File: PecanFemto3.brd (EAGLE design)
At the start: 28.9 x 17 mm, 43 parts, among them IC1 SPV1040T, IC3 EVA7M, IC4 SI4060/3, IC5 LPC824M201JHI33E, U1 TPS62203DBVT

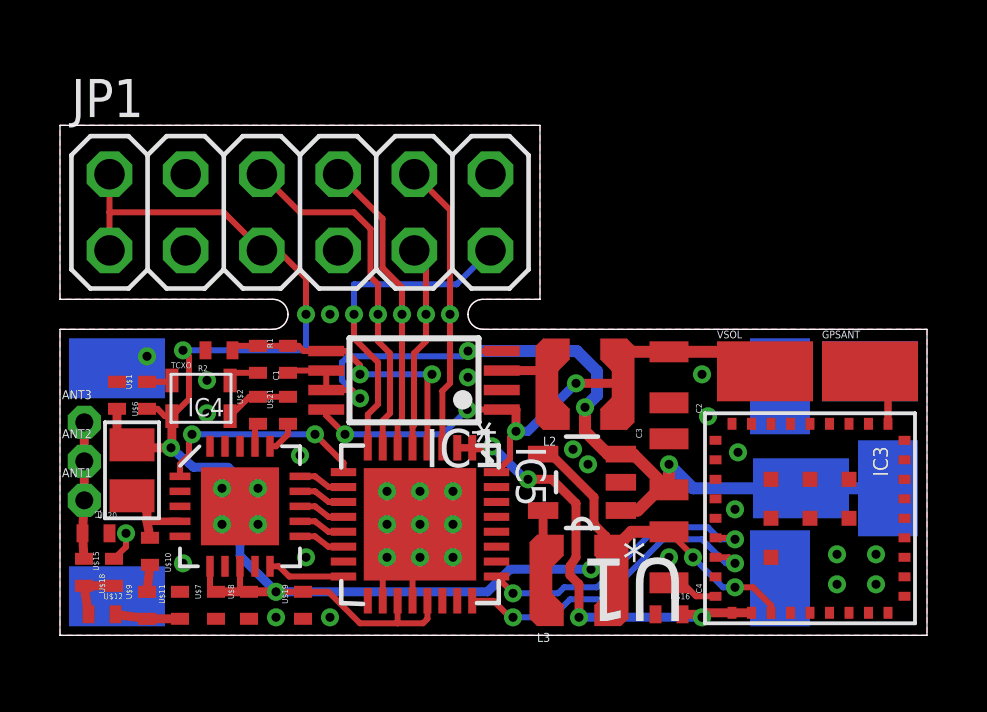
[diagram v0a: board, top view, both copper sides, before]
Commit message: Added LEDs, changed size of pinheader, moved parts
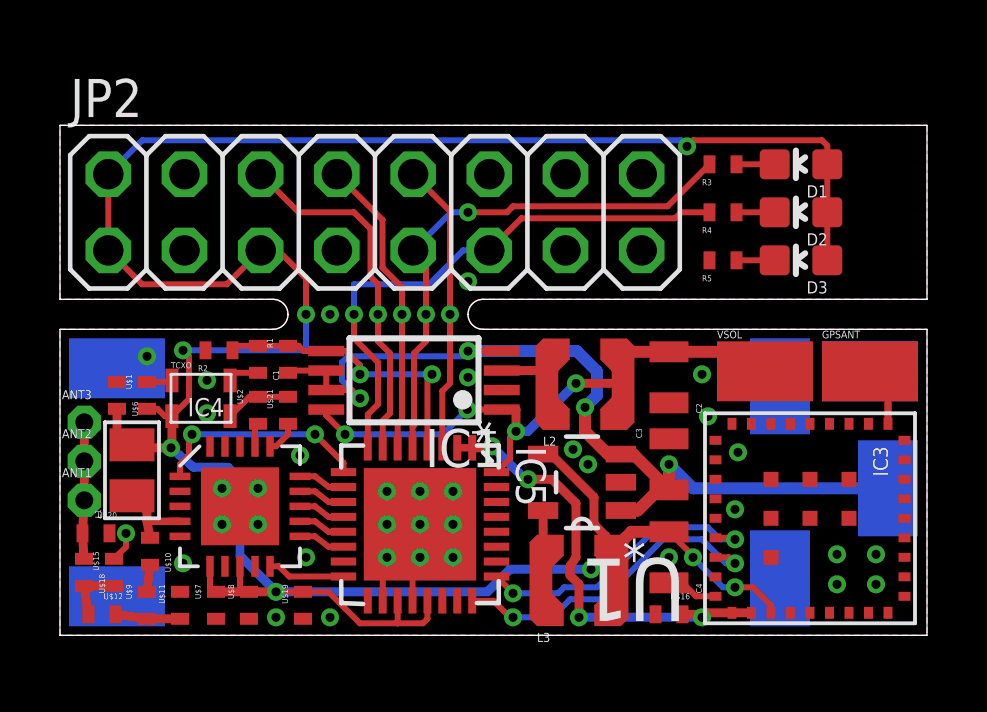
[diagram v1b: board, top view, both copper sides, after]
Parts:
- removed JP1: (no value), pinhead:2X06
- removed VBAT1: (no value), PecanFemto4:SMD1,27-2,54
- added D1, D2, D3: (no value), SparkFun-LED:LED-0603
- added JP2: (no value), pinhead:2X08
- added R3, R4, R5: 10k, PecanPico6:0402
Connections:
- new net N$11: D2.C, R4.P$2
- new net N$12: D3.C, R5.P$2
- new net N$8: D1.C, R3.P$2
- net GND: now also JP2.12, JP2.13, JP2.14, JP2.15, JP2.16, JP2.3, JP2.4, JP2.7, R5.P$1; no longer JP1.12, JP1.3, JP1.4, JP1.7
- net OUT1: now also JP2.9, R3.P$1; no longer JP1.9
- net OUT2: now also JP2.11, R4.P$1; no longer JP1.11
- net RESET: now also JP2.10; no longer JP1.10
- net SWCLK: now also JP2.8; no longer JP1.8
- net SWDIO: now also JP2.6; no longer JP1.6
- net VBAT: no longer VBAT1.1
- net VCC: now also D1.A, D2.A, D3.A, JP2.1, JP2.2, JP2.5; no longer JP1.1, JP1.2, JP1.5
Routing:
- net VCC: track 68.3 -> 97.2 mm, vias 7 -> 8
- net OUT1: track 6.93 -> 18.0 mm, vias 1 -> 2
- net OUT2: track 10.9 -> 18.8 mm
- net N$8: track 0.00 -> 1.27 mm
- net N$12: track 0.00 -> 1.27 mm
- net N$11: track 0.00 -> 1.27 mm
- net GND: vias 35 -> 36
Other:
- outline, holes or cut-outs redrawn
- board text added: "2015-Aug"
- board text added: "FLY HIGH!"
- board text added: "OUT1"
- board text added: "OUT2"
- board text added: "Pecan Femto 3"
- board text added: "VCC"

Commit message: Connected TCXO VCC to Si4464
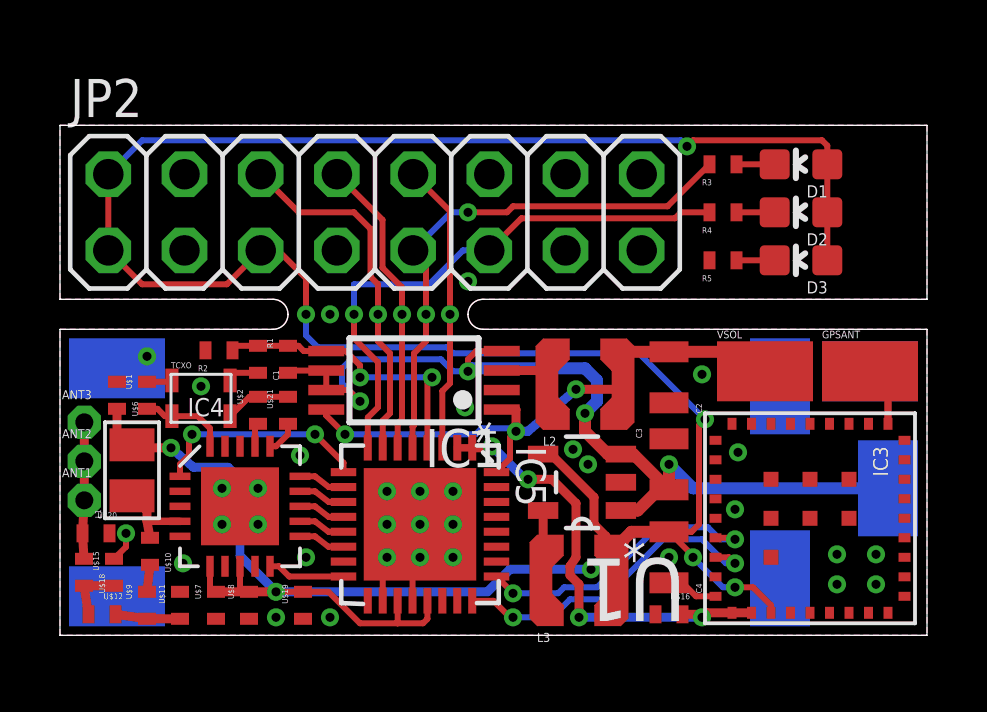
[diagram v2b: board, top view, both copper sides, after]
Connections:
- new net GPIO3: IC4.20, TCXO.4, U$1.P$2
- net VCC: no longer TCXO.4, U$1.P$2
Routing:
- net VCC: track 97.2 -> 107.2 mm
- net GPIO3: track 0.00 -> 2.97 mm
- net GND: track 9.55 -> 10.4 mm, vias 36 -> 34
- net VSOLAR: track 23.6 -> 23.8 mm, vias 4 -> 3

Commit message: Connected V_USB and RTC_I to GND
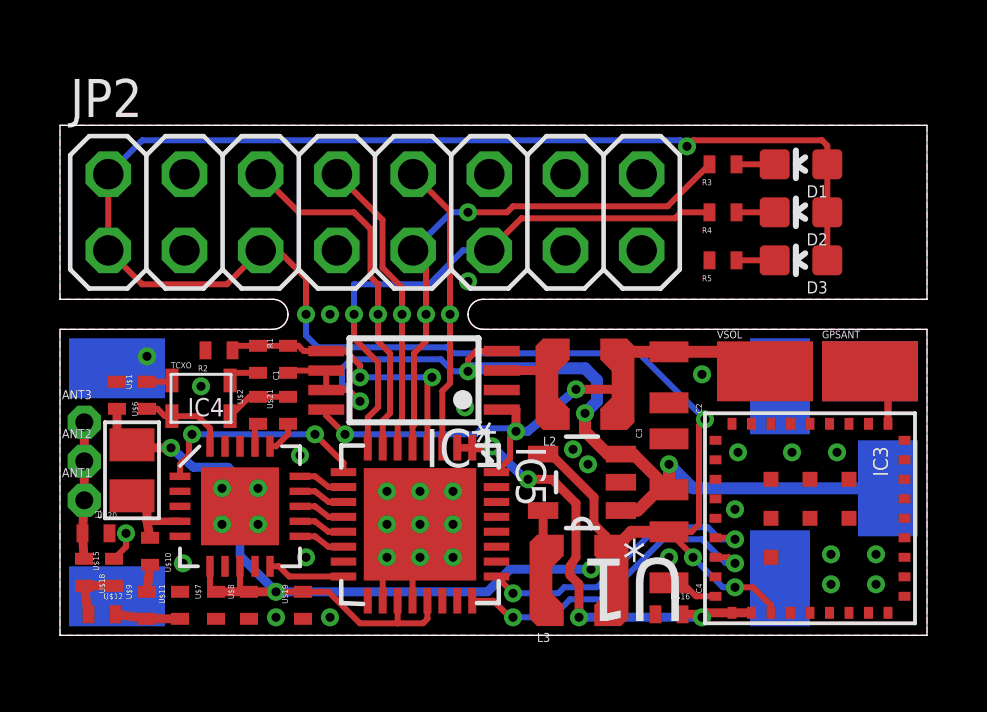
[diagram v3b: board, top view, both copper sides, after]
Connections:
- net GND: now also IC3.P$7, IC3.P$9
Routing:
- net GND: vias 34 -> 36
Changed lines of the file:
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@@
 <contactref element="GND24" pad="1"/>
 <contactref element="GND30" pad="1"/>
-<via x="40.4" y="16.7" extent="1-16" drill="0.3"/>
+<via x="40.2" y="16.7" extent="1-16" drill="0.3"/>
 <via x="41.7" y="16.7" extent="1-16" drill="0.3"/>
 <via x="41.7" y="17.7" extent="1-16" drill="0.3"/>
-<via x="40.4" y="17.7" extent="1-16" drill="0.3"/>
+<via x="40.2" y="17.7" extent="1-16" drill="0.3"/>
 <via x="37" y="19.2" extent="1-16" drill="0.3"/>
 <via x="37.1" y="21.1" extent="1-16" drill="0.3"/>
@@
 <via x="19.2" y="23.3" extent="1-16" drill="0.3"/>
 <wire x1="21.1" y1="19.9" x2="20.5" y2="19.3" width="0.2" layer="1"/>
+<contactref element="IC3" pad="P$7"/>
+<contactref element="IC3" pad="P$9"/>
+<via x="40.4" y="21.1" extent="1-16" drill="0.3"/>
+<via x="38.9" y="21.1" extent="1-16" drill="0.3"/>
 </signal>
 <signal name="N$4">

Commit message: Moved parts around
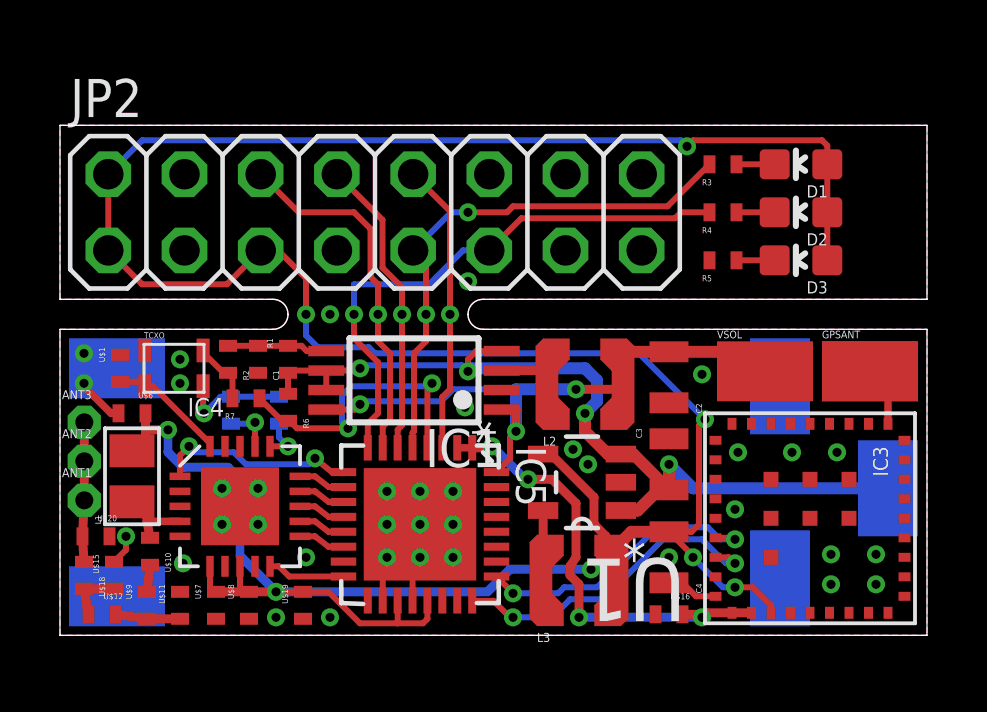
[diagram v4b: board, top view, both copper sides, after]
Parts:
- added R6: 22k, PecanPico6:0402
- added R7: 10k, PecanPico6:0402
- moved TCXO 1.35 mm to (18.3, 23.9)
- moved U$1 1.27 mm to (16.5, 23.9)
- moved U$2 0.90 mm to (20.2, 22.5), flipped to the bottom
- moved U$6 0.78 mm to (16.9, 22.4), turned to 180 degrees
- moved R2 0.42 mm to (20.1, 24.2), turned to 90 degrees
- moved U$21 0.30 mm to (21.8, 22.5), flipped to the bottom
- moved L1 0.20 mm to (16.9, 20.3)
- moved U$15 0.10 mm to (16.3, 17.0)
- moved U$18 0.10 mm to (15.3, 17.0)
- moved U$20 0.10 mm to (15.7, 18.3)
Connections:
- new net N$20: C1.P$2, IC1.5, R1.P$1, R2.P$2
- net GND: now also R7.P$1
- net VBAT: now also R6.P$2
- net VBAT_DIFF: now also R6.P$1, R7.P$2; no longer C1.P$2, IC1.5, R1.P$1, R2.P$2
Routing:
- net N$20: track 0.00 -> 3.35 mm
- net GND: track 10.4 -> 12.1 mm, vias 36 -> 37
- net N$9: track 2.20 -> 3.65 mm, vias 0 -> 1
- net VBAT: track 31.1 -> 29.7 mm
- net GPIO3: track 2.97 -> 4.03 mm
- net N$7: track 0.85 -> 1.62 mm, vias 0 -> 1
- net VSOLAR: track 23.8 -> 24.4 mm
- net RADIO_SDN: track 7.32 -> 6.77 mm
- net N$10: track 1.12 -> 1.47 mm, vias 0 -> 1
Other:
- board text added: "GND"
- board text added: "VBAT"
- board text added: "XIN"
- board text added: "XOUT"

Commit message: Moved parts around
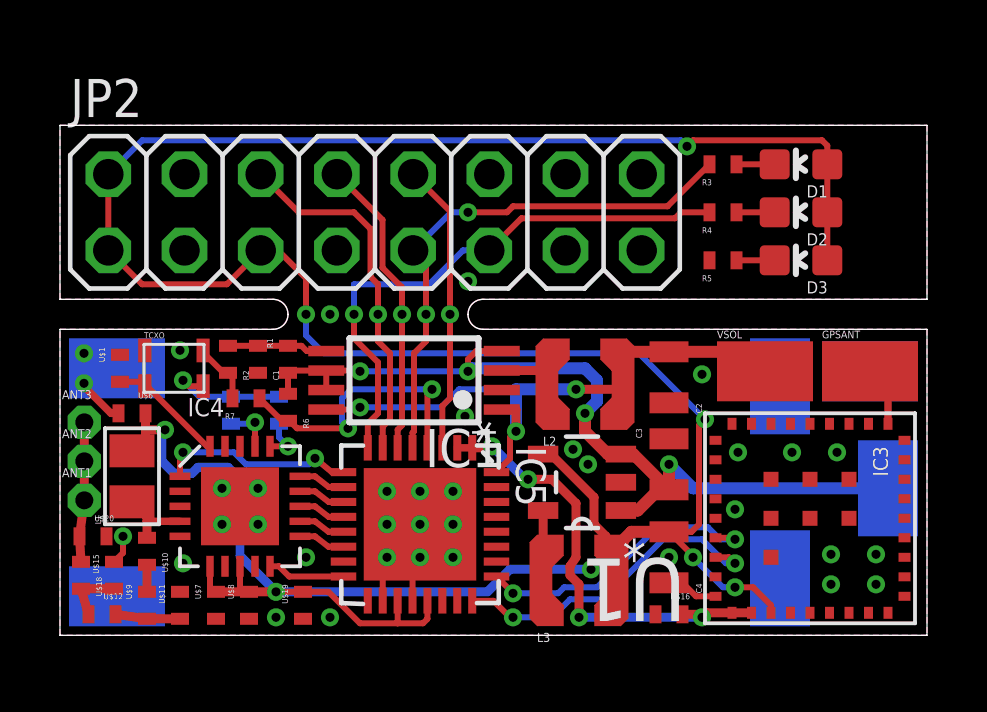
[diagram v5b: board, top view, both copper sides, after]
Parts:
- moved U$10 0.10 mm to (17.4, 17.8)
- moved U$18 0.10 mm to (15.2, 17.0)
- moved U$20 0.10 mm to (15.6, 18.3)
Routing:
- net N$9: track 3.65 -> 4.18 mm
- net GND: track 12.1 -> 12.0 mm, vias 37 -> 36

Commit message: Moved parts around, updated GERBERs
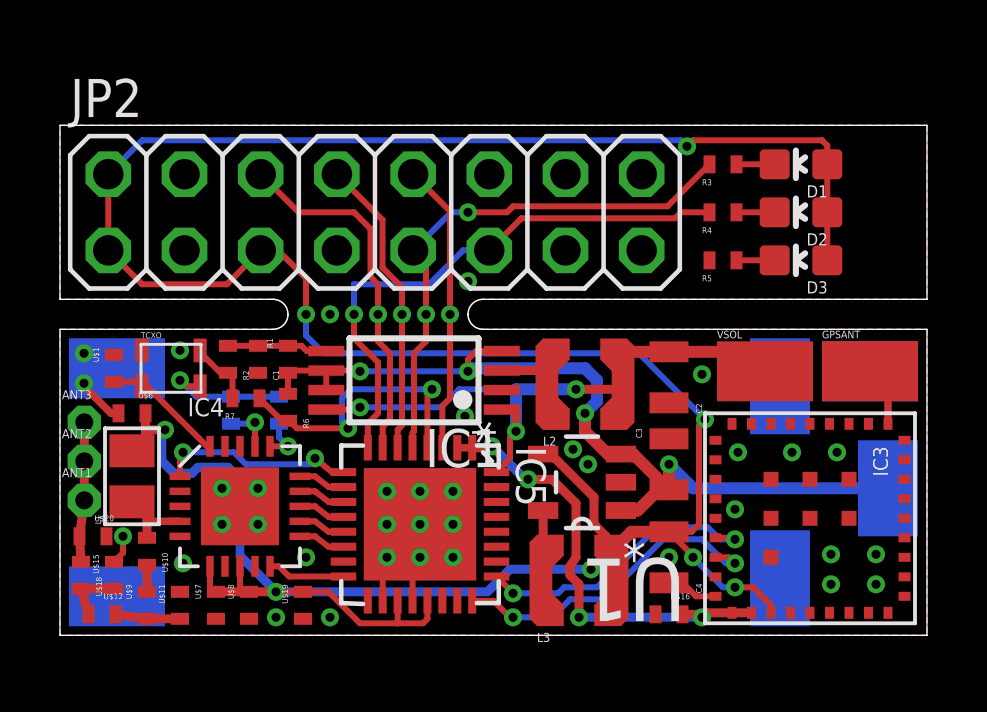
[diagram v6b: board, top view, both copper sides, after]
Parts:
- moved U$1 0.20 mm to (16.3, 23.9)
- moved TCXO 0.10 mm to (18.2, 23.9)
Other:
- board text added: "Pecan Femto3"
- board text removed: "Pecan Femto 3"
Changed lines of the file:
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@@
 <grid distance="0.1" unitdist="mm" unit="mm" style="lines" multiple="1" display="yes" altdistance="0.025" altunitdist="inch" altunit="inch"/>
 <layers>
-<layer number="1" name="Top" color="4" fill="1" visible="yes" active="yes"/>
+<layer number="1" name="Top" color="4" fill="1" visible="no" active="yes"/>
 <layer number="16" name="Bottom" color="1" fill="1" visible="yes" active="yes"/>
 <layer number="17" name="Pads" color="2" fill="1" visible="yes" active="yes"/>
@@
 <layer number="19" name="Unrouted" color="6" fill="1" visible="yes" active="yes"/>
 <layer number="20" name="Dimension" color="15" fill="1" visible="yes" active="yes"/>
-<layer number="21" name="tPlace" color="7" fill="1" visible="yes" active="yes"/>
+<layer number="21" name="tPlace" color="7" fill="1" visible="no" active="yes"/>
 <layer number="22" name="bPlace" color="7" fill="1" visible="yes" active="yes"/>
-<layer number="23" name="tOrigins" color="15" fill="1" visible="yes" active="yes"/>
+<layer number="23" name="tOrigins" color="15" fill="1" visible="no" active="yes"/>
 <layer number="24" name="bOrigins" color="15" fill="1" visible="yes" active="yes"/>
-<layer number="25" name="tNames" color="7" fill="1" visible="yes" active="yes"/>
-<layer number="26" name="bNames" color="7" fill="1" visible="yes" active="yes"/>
+<layer number="25" name="tNames" color="7" fill="1" visible="no" active="yes"/>
+<layer number="26" name="bNames" color="7" fill="1" visible="no" active="yes"/>
 <layer number="27" name="tValues" color="7" fill="1" visible="no" active="yes"/>
 <layer number="28" name="bValues" color="7" fill="1" visible="no" active="yes"/>
@@
 <layer number="49" name="Reference" color="7" fill="1" visible="yes" active="yes"/>
 <layer number="50" name="dxf" color="7" fill="1" visible="no" active="no"/>
-<layer number="51" name="tDocu" color="7" fill="1" visible="yes" active="yes"/>
+<layer number="51" name="tDocu" color="7" fill="1" visible="no" active="yes"/>
 <layer number="52" name="bDocu" color="7" fill="1" visible="yes" active="yes"/>
 <layer number="53" name="tGND_GNDA" color="7" fill="1" visible="no" active="no"/>
@@
 <text x="41" y="27.2" size="0.55" layer="51">VCC</text>
 <text x="43.1" y="27.9" size="1.5" layer="52" rot="SMR0">Pecan
-Femto 3</text>
+Femto3</text>
 <text x="43.1" y="26.7" size="0.8" layer="52" rot="MR0">2015-Aug</text>
 <text x="28.8" y="15.3" size="0.7" layer="52" rot="MR0">FLY HIGH!</text>
-<text x="19.8" y="24" size="0.5" layer="52" rot="MR180">XIN</text>
-<text x="21.5" y="24" size="0.5" layer="52" rot="MR180">XOUT</text>
+<text x="19.5" y="24" size="0.5" layer="52" rot="MR180">XIN</text>
+<text x="21" y="24" size="0.5" layer="52" rot="MR180">XOUT</text>
 <text x="16.3" y="22.7" size="0.5" layer="52" rot="MR180">GND</text>
 <text x="18.3" y="15.3" size="0.5" layer="52" rot="MR90">GND</text>
@@
 <element name="GPSANT" library="PecanFemto4" package="SMD1,27-2,54" value="" x="41.5" y="23.8" rot="R270"/>
 <element name="GND29" library="PecanFemto4" package="SMD1,27-2,54" value="" x="41.5" y="23.8" rot="MR270"/>
-<element name="U$1" library="sven" package="0402" value="100nF" x="16.5" y="23.9" rot="R270"/>
-<element name="TCXO" library="tcxo" package="TCXO_2.0X1.6" value="TXC 7Z-26.000MCG-T" x="18.3" y="23.9"/>
+<element name="U$1" library="sven" package="0402" value="100nF" x="16.3" y="23.9" rot="R270"/>
+<element name="TCXO" library="tcxo" package="TCXO_2.0X1.6" value="TXC 7Z-26.000MCG-T" x="18.2" y="23.9"/>
 <element name="VBAT" library="PecanFemto4" package="SMD1,27-2,54" value="" x="42.1" y="19.9" rot="MR0"/>
 <element name="U$2" library="sven" package="0402" value="100pF" x="20.2" y="22.5" rot="MR270"/>
@@
 <via x="38.9" y="21.1" extent="1-16" drill="0.3"/>
 <contactref element="R7" pad="P$1"/>
-<wire x1="19.27" y1="24.495" x2="19.27" y2="24.43" width="0.2" layer="1"/>
-<wire x1="19.27" y1="24.43" x2="19.95" y2="23.75" width="0.2" layer="1"/>
-<wire x1="19.95" y1="23.75" x2="20.1" y2="23.75" width="0.2" layer="1"/>
+<wire x1="19.17" y1="24.495" x2="19.17" y2="24.43" width="0.2" layer="1"/>
+<wire x1="19.17" y1="24.43" x2="19.85" y2="23.75" width="0.2" layer="1"/>
+<wire x1="19.85" y1="23.75" x2="20.1" y2="23.75" width="0.2" layer="1"/>
 <wire x1="20.1" y1="23.75" x2="20.25" y2="23.6" width="0.2" layer="1"/>
 <wire x1="20.25" y1="23.6" x2="20.25" y2="22.9" width="0.2" layer="1"/>
@@
 <contactref element="TCXO" pad="3"/>
 <contactref element="U$2" pad="P$1"/>
-<via x="18.6" y="23.5" extent="1-16" drill="0.3"/>
-<wire x1="18.6" y1="23.5" x2="19.15" y2="22.95" width="0.2" layer="16"/>
-<wire x1="19.15" y1="22.95" x2="20.2" y2="22.95" width="0.2" layer="16"/>
+<via x="18.5" y="23.5" extent="1-16" drill="0.3"/>
+<wire x1="18.5" y1="23.5" x2="19.05" y2="22.95" width="0.2" layer="16"/>
+<wire x1="19.05" y1="22.95" x2="20.2" y2="22.95" width="0.2" layer="16"/>
 <wire x1="20.2" y1="22.95" x2="21.8" y2="22.95" width="0.2" layer="16"/>
-<wire x1="18.6" y1="23.5" x2="18.795" y2="23.305" width="0.2" layer="1"/>
-<wire x1="18.795" y1="23.305" x2="19.27" y2="23.305" width="0.2" layer="1"/>
+<wire x1="18.5" y1="23.5" x2="18.695" y2="23.305" width="0.2" layer="1"/>
+<wire x1="18.695" y1="23.305" x2="19.17" y2="23.305" width="0.2" layer="1"/>
 </signal>
 <signal name="N$10">
@@
 <contactref element="U$1" pad="P$2"/>
 <contactref element="TCXO" pad="4"/>
-<wire x1="17.33" y1="23.305" x2="17.33" y2="23.45" width="0.2" layer="1"/>
-<wire x1="17.33" y1="23.45" x2="16.5" y2="23.45" width="0.2" layer="1"/>
-<wire x1="17.33" y1="23.305" x2="17.395" y2="23.305" width="0.2" layer="1"/>
+<wire x1="17.23" y1="23.305" x2="17.33" y2="23.45" width="0.2" layer="1"/>
+<wire x1="17.33" y1="23.45" x2="16.3" y2="23.45" width="0.2" layer="1"/>
+<wire x1="17.23" y1="23.305" x2="17.395" y2="23.305" width="0.2" layer="1"/>
 <wire x1="17.395" y1="23.305" x2="19.4" y2="21.3" width="0.2" layer="1"/>
 <wire x1="19.4" y1="21.3" x2="19.5" y2="21.3" width="0.2" layer="1"/>

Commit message: Changed naming of parts
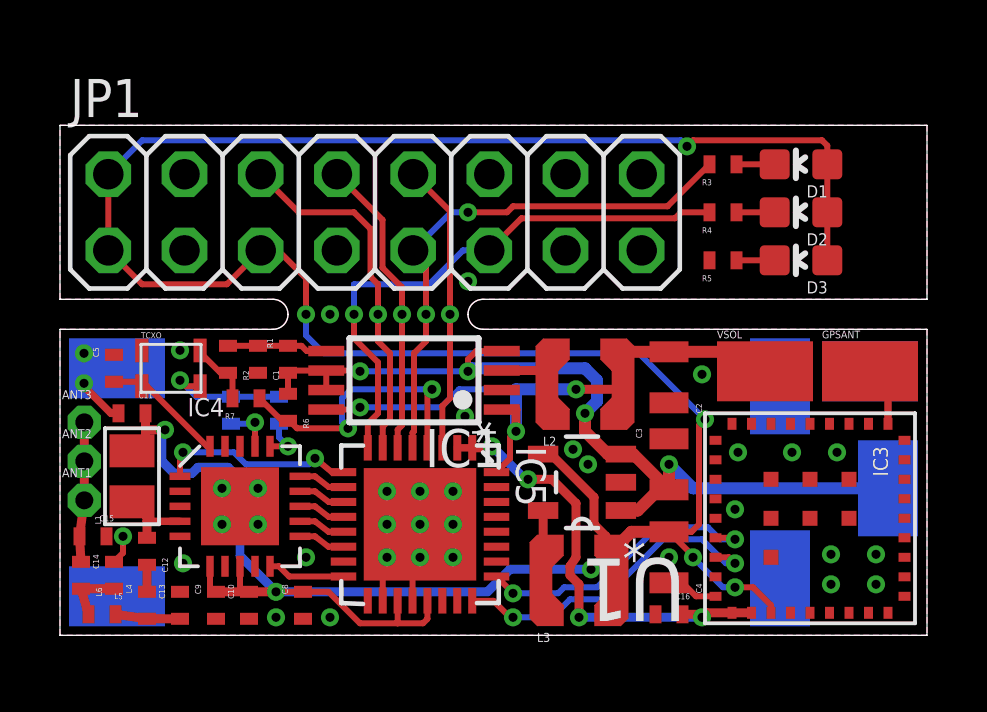
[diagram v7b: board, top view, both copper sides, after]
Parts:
- C11, C12: value CAP-0402 -> 470pF
- C13: value CAP-0402 -> 18pF
- C14, C15: value CAP-0402 -> 22pF
- L1: value (none) -> 470nH
- L4: value IND-0402 -> 56nH
- L5, L6: value IND-0402 -> 68nH
- renumbered JP2 to JP1, U$1 to C5, U$10 to C12, U$11 to C13, U$12 to L5, U$15 to C14, U$16 to C16, U$18 to L6, U$19 to C8, U$2 to C7, U$20 to C15, U$21 to C6, U$6 to C11, U$7 to C9, U$8 to C10, U$9 to L4
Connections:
- net N$4 renamed C12
- net N$5 renamed L5
